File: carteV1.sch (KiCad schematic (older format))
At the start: 48 parts, among them CON1 USB-MINI-B, J12 FILTER_IOUT_DUT2, J6 REF_CLK_DUT2, J7 CRYSTAL OUTDUT2, T4 BALUN, T8 T1-1T, U1 AD9954, U2 LM1117MP-1.8, U3 LM1117MP-1.8, U4 LM1117MP-3.3, U5 MCP2210-SO, X1 25mhz, X2 12mhz

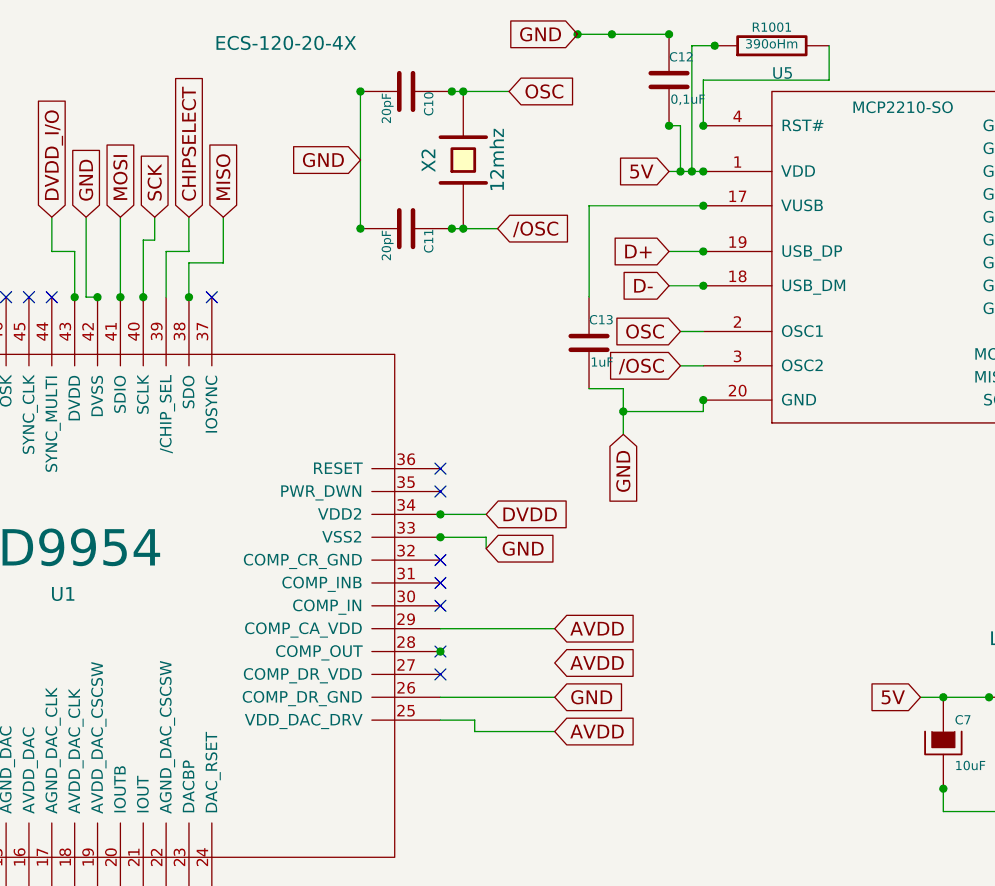
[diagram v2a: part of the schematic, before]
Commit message: Add MP2210 documentation and supply MP2210 with 3,3V
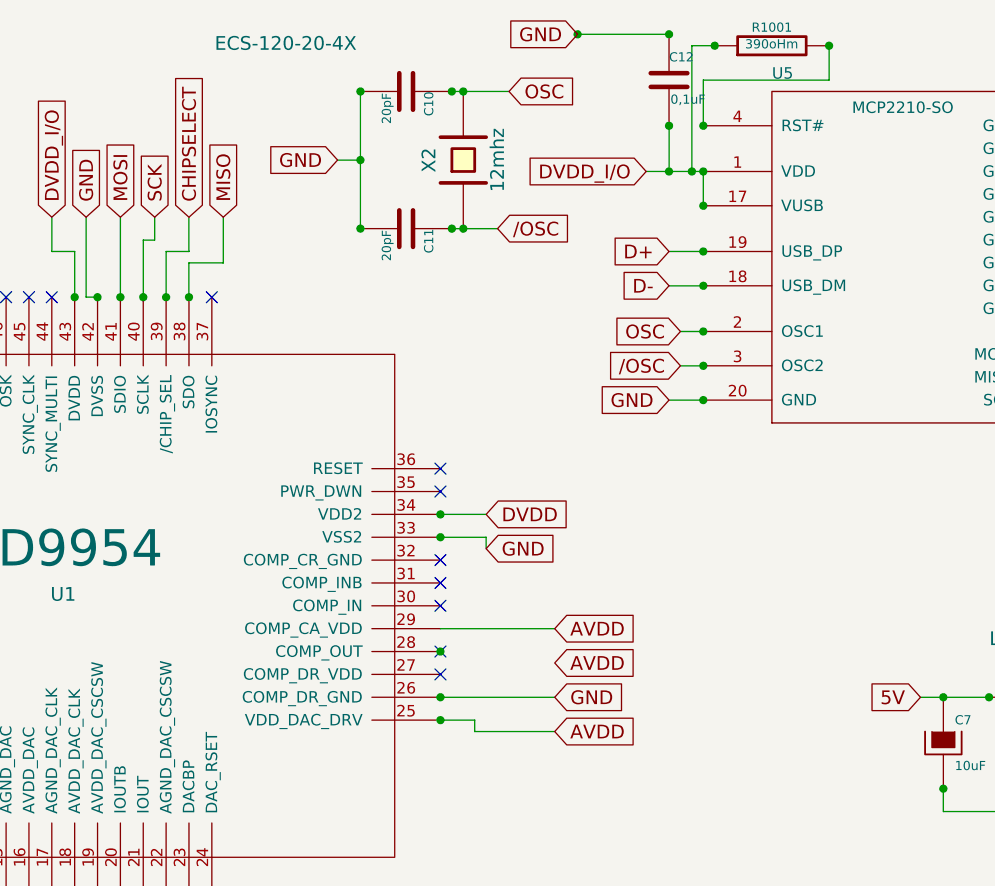
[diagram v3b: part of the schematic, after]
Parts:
- removed C13: 1uF, symbol C
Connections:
- net 5V: no longer C12.2, R1001.1, U5.1 (VDD)
- net DVDD_I/O: now also C12.2, R1001.1, U5.1 (VDD), U5.17 (VUSB)
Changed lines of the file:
@@
 	1    0    0    -1
 $EndComp
-Text GLabel 6850 1150 0    60   Input ~ 0
+Text GLabel 6750 1150 0    60   Input ~ 0
 GND
 $Comp
@@
 Text GLabel 5950 1400 1    60   Input ~ 0
 SCK
-Text GLabel 8200 1200 0    60   Input ~ 0
-5V
 $Comp
 L C C12
@@
 	1    0    0    -1
 $EndComp
-$Comp
-L C C13
-U 1 1 537AD513
-P 7850 1950
-F 0 "C13" H 7850 2050 40  0000 L CNN
-F 1 "1uF" H 7856 1865 40  0000 L CNN
-F 2 "" H 7888 1800 30  0000 C CNN
-F 3 "~" H 7850 1950 60  0000 C CNN
-	1    7850 1950
-	1    0    0    -1
-$EndComp
-Text GLabel 8000 2350 3    60   Input ~ 0
+Text GLabel 8200 2200 0    60   Input ~ 0
 GND
 Text GLabel 10400 1000 2    60   Input ~ 0
@@
 Wire Wire Line
 	8250 1900 8350 1900
-Wire Wire Line
-	7850 1350 8350 1350
-Wire Wire Line
-	7850 1750 7850 1350
-Wire Wire Line
-	8000 2150 7850 2150
-Connection ~ 8350 2200
-Connection ~ 8000 2250
-Wire Wire Line
-	8000 2150 8000 2350
 Connection ~ 8350 1000
 Connection ~ 8400 650
@@
 	8300 1200 8300 650
 Connection ~ 8200 600
-Connection ~ 7950 600
 Connection ~ 7800 600
-Connection ~ 8200 1000
 Connection ~ 8350 1350
-Connection ~ 8250 1200
-Wire Wire Line
-	8250 1000 8250 1200
-Wire Wire Line
-	8200 1000 8250 1000
-Wire Wire Line
-	7800 600  8200 600
 Connection ~ 8350 1200
 Wire Wire Line
-	8200 1200 8350 1200
+	8100 1200 8350 1200
 Connection ~ 8350 1550
 Connection ~ 8350 1700
@@
 Wire Wire Line
 	8200 1550 8350 1550
-Wire Wire Line
-	8350 2250 8350 2200
-Wire Wire Line
-	8000 2250 8350 2250
 Connection ~ 10050 1000
 Wire Wire Line
@@
 Wire Wire Line
 	3800 2450 3950 2450
+Wire Wire Line
+	8200 2200 8350 2200
+Connection ~ 8350 2200
+Connection ~ 8350 2050
+Connection ~ 8350 1900
+Connection ~ 8900 650
+Text GLabel 8100 1200 0    60   Input ~ 0
+DVDD_I/O
+Wire Wire Line
+	8350 1200 8350 1350
+Wire Wire Line
+	7800 600  8200 600
+Wire Wire Line
+	8200 1000 8200 1200
+Connection ~ 8200 1200
+Connection ~ 8200 1000
+Wire Wire Line
+	6750 1150 6850 1150
+Connection ~ 6850 1150
+Connection ~ 6000 1750
+Connection ~ 7200 3500
+Connection ~ 7200 3600
 $EndSCHEMATC

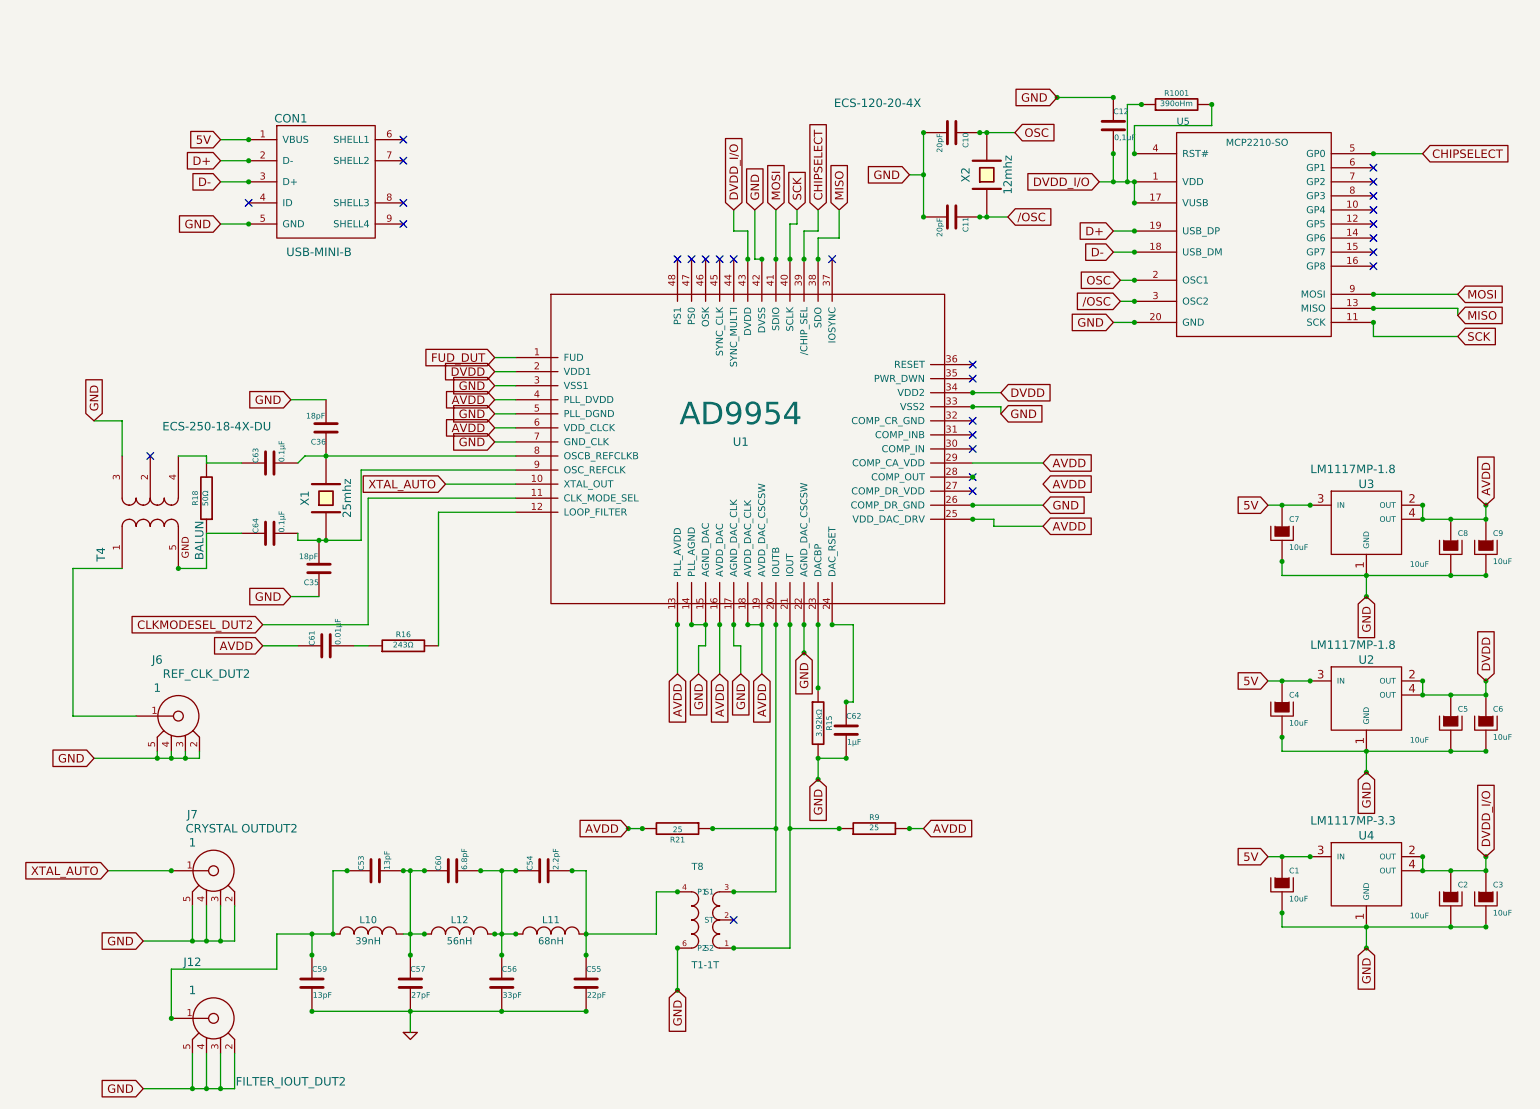
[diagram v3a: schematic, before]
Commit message: Ajout jumper
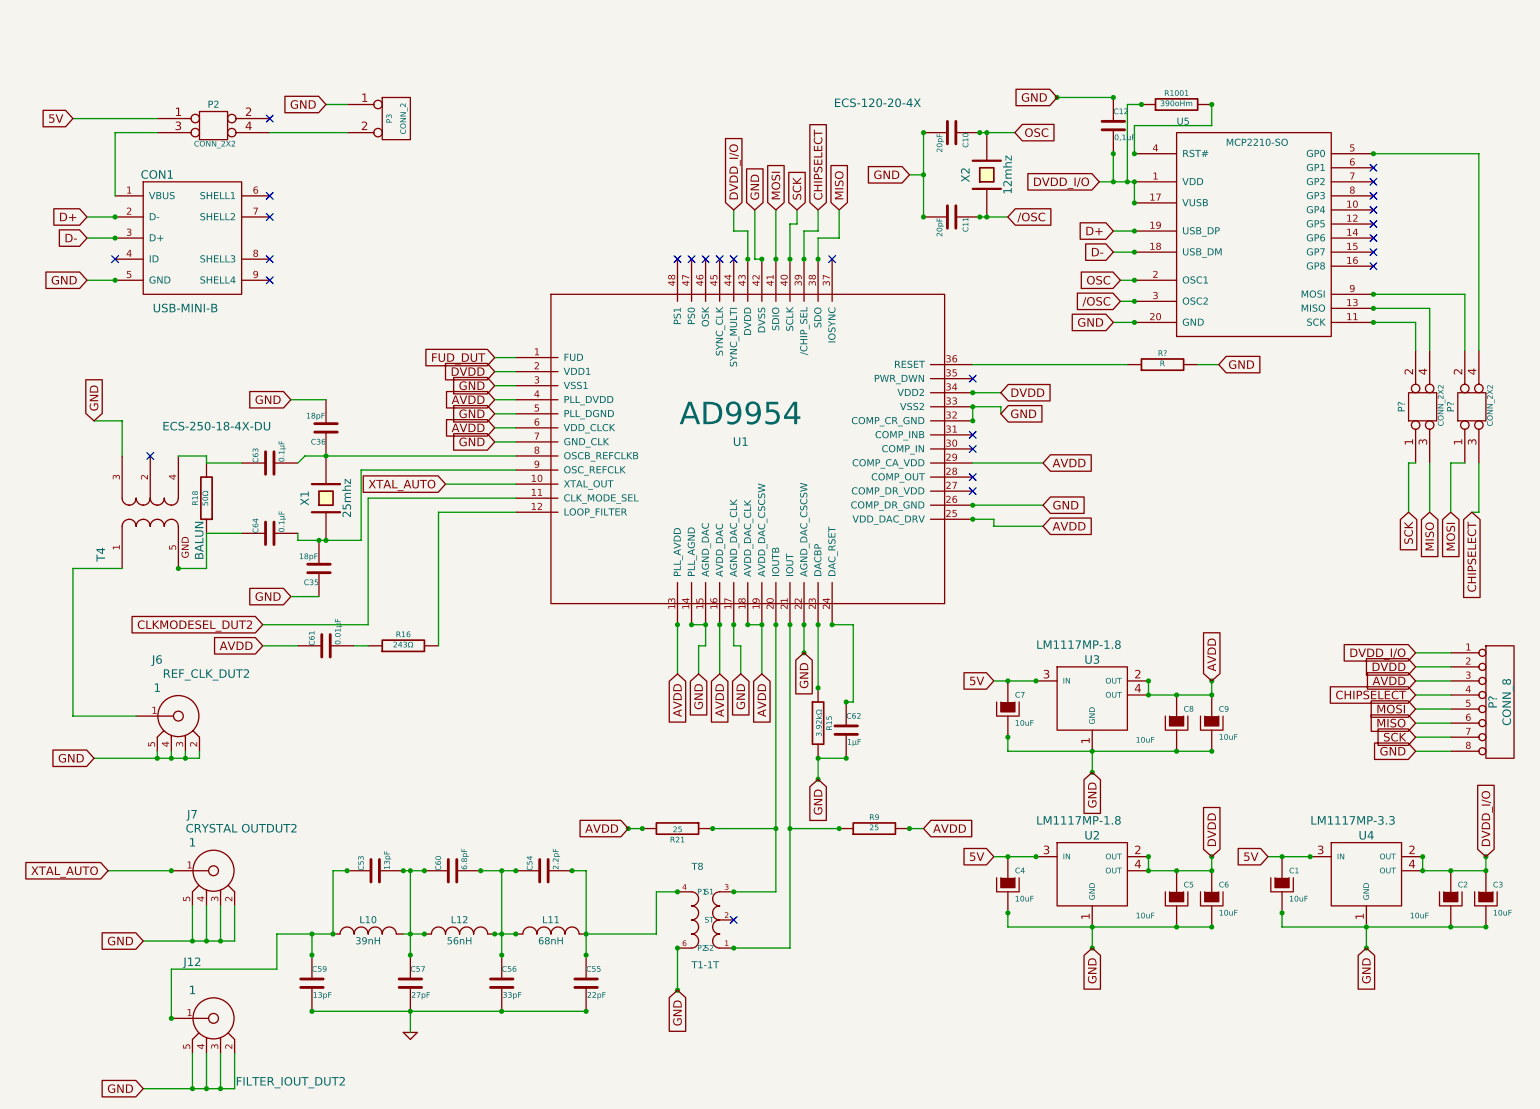
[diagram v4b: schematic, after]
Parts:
- added P2, P? (x2): CONN_2X2, symbol CONN_2X2
- added P3: CONN_2, symbol CONN_2
- added P?: CONN_8, symbol CONN_8
- added R?: R, ~, symbol R
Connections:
- net 5V: now also P2.1; no longer CON1.1 (VBUS)
- net AVDD: now also P?.3 (P3)
- net CHIPSELECT: now also P?.3, P?.4 (P4); no longer U5.5 (GP0)
- net DVDD: now also P?.2 (P2)
- net DVDD_I/O: now also P?.1 (P1)
- net GND: now also U1.32 (COMP_CR_GND), P3.1 (P1), P?.8 (P8), R?.2
- net MISO: now also P?.3, P?.6 (P6); no longer U5.13 (MISO)
- net MOSI: now also P?.1, P?.5 (P5); no longer U5.9 (MOSI)
- net SCK: now also P?.1, P?.7 (P7); no longer U5.11 (SCK)
- net at U1.36 (RESET): now also R?.1
- new net: CON1.1 (VBUS), P2.3
- new net: P?.2, U5.11 (SCK)
- new net: P?.4, U5.13 (MISO)
- new net: P?.4, U5.5 (GP0)
- new net: P?.2, U5.9 (MOSI)
- new net: P2.4, P3.2 (PM)
- no-connect marks 28 -> 27
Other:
- moved on the sheet: C4, C5, C6, C7, C8, C9, CON1, U2, U3

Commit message: modification ad9954
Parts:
- R?: value R -> 3900
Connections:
- net GND: now also U1.30 (COMP_IN), U1.31 (COMP_INB), U1.35 (PWR_DWN), U1.37 (IOSYNC), U1.46 (OSK), U1.47 (PS0), U1.48 (PS1)
- no-connect marks 27 -> 20
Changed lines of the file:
@@
 Sheet 1 1
 Title "AD9954 - GENERATION SIGNAL HF"
-Date "25 may 2014"
+Date "26 may 2014"
 Rev "0.1"
 Comp "Polytech'Tours"
@@
 Text GLabel 7450 1450 2    60   Input ~ 0
 /OSC
-NoConn ~ 7200 2600
-NoConn ~ 7200 3000
-NoConn ~ 7200 3100
-NoConn ~ 5100 1750
-NoConn ~ 5200 1750
-NoConn ~ 5300 1750
-NoConn ~ 5400 1750
-NoConn ~ 5500 1750
-NoConn ~ 6200 1750
 NoConn ~ 7200 3300
 NoConn ~ 7200 3400
@@
 	0    -1   -1   0
 $EndComp
+$Comp
+L R R?
+U 1 1 53822BF5
+P 8550 2500
+F 0 "R?" V 8630 2500 40  0000 C CNN
+F 1 "3900" V 8557 2501 40  0000 C CNN
+F 2 "~" V 8480 2500 30  0000 C CNN
+F 3 "~" H 8550 2500 30  0000 C CNN
+	1    8550 2500
+	0    -1   -1   0
+$EndComp
+Text GLabel 8950 2500 2    60   Input ~ 0
+GND
+Text GLabel 5200 1400 1    60   Input ~ 0
+GND
 Wire Wire Line
 	8250 2050 8350 2050
@@
 Connection ~ 4450 6700
 Wire Wire Line
-	6850 1450 6850 850
+	6850 850  6850 1750
 Wire Wire Line
 	7250 850  7500 850
@@
 Wire Wire Line
 	10800 1000 10800 2400
-$Comp
-L R R?
-U 1 1 53822BF5
-P 8550 2500
-F 0 "R?" V 8630 2500 40  0000 C CNN
-F 1 "R" V 8557 2501 40  0000 C CNN
-F 2 "~" V 8480 2500 30  0000 C CNN
-F 3 "~" H 8550 2500 30  0000 C CNN
-	1    8550 2500
-	0    -1   -1   0
-$EndComp
 Wire Wire Line
 	7200 2500 8300 2500
-Text GLabel 8950 2500 2    60   Input ~ 0
-GND
 Wire Wire Line
 	8800 2500 8950 2500
 Wire Wire Line
-	7200 2900 7200 2800
+	7200 2800 7200 3100
 Connection ~ 7200 2900
+Wire Wire Line
+	5200 1750 5200 1400
+Wire Wire Line
+	5100 1750 5100 1400
+Wire Wire Line
+	5100 1400 5300 1400
+Connection ~ 5200 1750
+Connection ~ 5100 1750
+Wire Wire Line
+	5300 1400 5300 1750
+Connection ~ 5200 1400
+Connection ~ 5300 1750
+Connection ~ 6800 1500
+NoConn ~ 5400 1750
+NoConn ~ 5500 1750
+Wire Wire Line
+	6850 1750 6200 1750
+Connection ~ 6200 1750
+Wire Wire Line
+	7200 2600 8900 2600
+Wire Wire Line
+	8900 2600 8900 2500
+Connection ~ 8900 2500
+Connection ~ 7200 2600
+Connection ~ 7200 2500
+Connection ~ 7200 3000
+Connection ~ 7200 3100
 $EndSCHEMATC
